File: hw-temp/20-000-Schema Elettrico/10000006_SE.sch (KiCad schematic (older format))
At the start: 36 parts, among them P1 CONN_01X04, P2 CONN_01X04, P3 CONN_01X04, P4 CONN_01X04, P5 CONN_01X04, P6 CONN_01X04, P7 CONN_01X04, P8 CONN_01X04, U1 TPS709, U2 PCA9306DC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

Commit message: aggiornamento completo libreria e schematico per generazione BOM
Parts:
- removed C1: 1u, symbol C
- removed C2: 3.3u, symbol C
- removed C3, C5, C7, C8, C9: 100n, symbol C
- removed C4, C6: 100p, symbol C
- removed P1, P2, P3, P4, P5, P6, P7, P8: CONN_01X04, symbol CONN_01X04
- added C1: C_1u_0603_10_X7R_25V, Capacitors_SMD:C_0603, symbol C_1u_0603_10_X7R_25V
- added C2: C_3u3_0603_10_X5R_10V, Capacitors_SMD:C_0603, symbol C_3u3_0603_10_X5R_10V
- added C3, C5, C7, C8, C9: C_100n_0603_10_X7R_25V, Capacitors_SMD:C_0603, symbol C_100n_0603_10_X7R_25V
- added C4, C6: C_100p_0603_5_NP0_50V, Capacitors_SMD:C_0603, symbol C_100p_0603_5_NP0_50V
- added P1, P2, P3, P4, P5, P6, P7, P8: PLUG_01X04_254, Socket_Strips:Socket_Strip_Straight_1x04, symbol PLUG_01X04_254
- U1: footprint (none) -> TO_SOT_Packages_SMD:SOT-23-5; MF (none) -> TI; MF_PN (none) -> TPS709; NOPOP (none) -> 0; VAL (none) -> TPS709
- U2: footprint (none) -> Housings_SSOP:TSSOP-8_3x3mm_Pitch0.65mm; MF (none) -> TI; MF_PN (none) -> PCA9306DCUR; NOPOP (none) -> 0; VAL (none) -> PCA9306DC
- U3: footprint (none) -> Housings_SSOP:TSSOP-16_4.4x5mm_Pitch0.65mm; MF (none) -> NXP; MF_PN (none) -> SC18IS602BIPW,128; NOPOP (none) -> 0; VAL (none) -> SC18IS602BIPW
- U4: footprint (none) -> Housings_SSOP:SSOP-20_5.3x7.2mm_Pitch0.65mm; MF (none) -> Maxim; MF_PN (none) -> MAX31865AAP+; NOPOP (none) -> 0; VAL (none) -> MAX31865

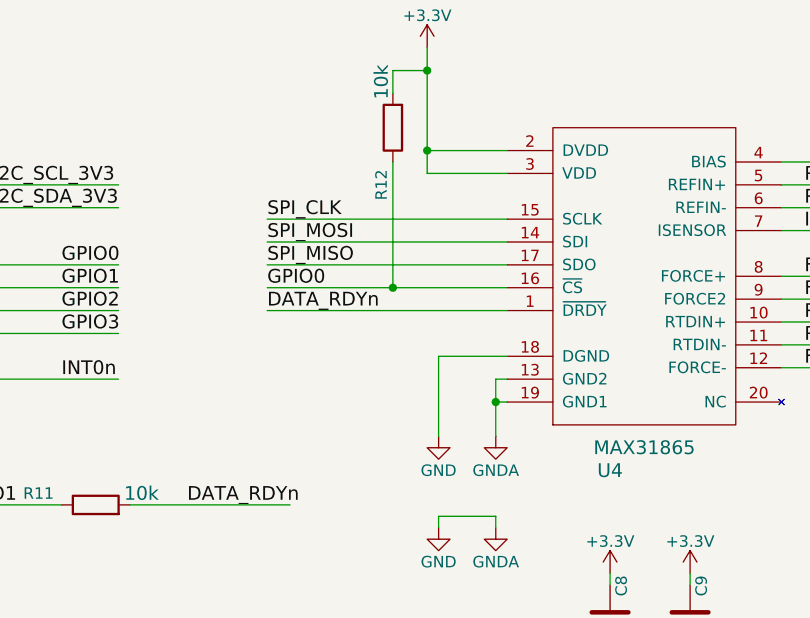
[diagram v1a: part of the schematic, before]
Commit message: Piazzamento scheda iniziato
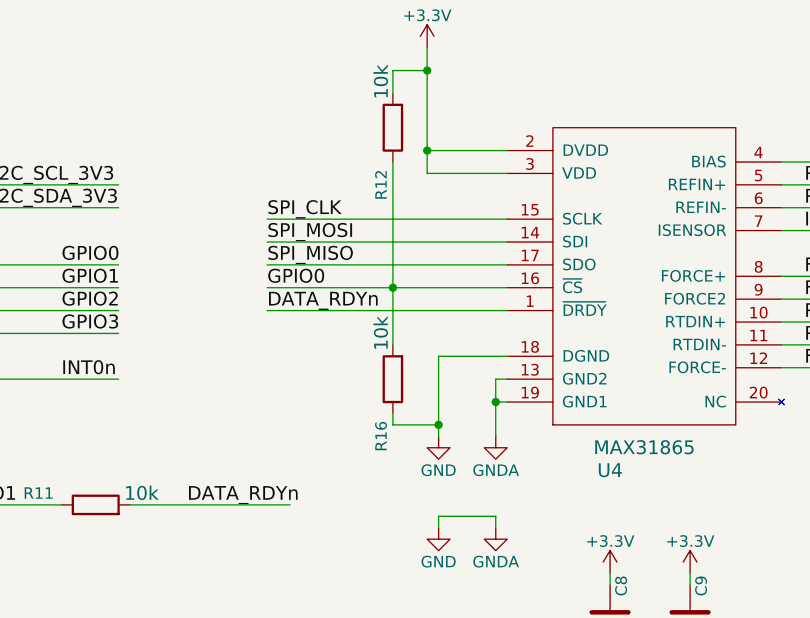
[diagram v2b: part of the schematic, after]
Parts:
- added R16: R_10K_0603_5, Resistors_SMD:R_0603, symbol R_10K_0603_5
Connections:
- wire segments 153 -> 155
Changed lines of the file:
@@
 01
 $Comp
-L GND #PWR01
+L GND #PWR7
 U 1 1 568A9F3F
 P 2050 2350
-F 0 "#PWR01" H 2050 2100 50  0001 C CNN
+F 0 "#PWR7" H 2050 2100 50  0001 C CNN
 F 1 "GND" H 2050 2200 50  0000 C CNN
 F 2 "" H 2050 2350 50  0000 C CNN
@@
 $EndComp
 $Comp
-L +3.3V #PWR02
+L +3.3V #PWR6
 U 1 1 568A9F53
 P 2050 2000
-F 0 "#PWR02" H 2050 1850 50  0001 C CNN
+F 0 "#PWR6" H 2050 1850 50  0001 C CNN
 F 1 "+3.3V" H 2050 2140 50  0000 C CNN
 F 2 "" H 2050 2000 50  0000 C CNN
@@
 $EndComp
 $Comp
-L +5V #PWR03
+L +5V #PWR5
 U 1 1 568A9F67
 P 2050 1650
-F 0 "#PWR03" H 2050 1500 50  0001 C CNN
+F 0 "#PWR5" H 2050 1500 50  0001 C CNN
 F 1 "+5V" H 2050 1790 50  0000 C CNN
 F 2 "" H 2050 1650 50  0000 C CNN
@@
 $EndComp
 $Comp
-L PWR_FLAG #FLG04
+L PWR_FLAG #FLG2
 U 1 1 568A9F7B
 P 1700 2000
-F 0 "#FLG04" H 1700 2095 50  0001 C CNN
+F 0 "#FLG2" H 1700 2095 50  0001 C CNN
 F 1 "PWR_FLAG" H 1700 2180 50  0000 C CNN
 F 2 "" H 1700 2000 50  0000 C CNN
@@
 $EndComp
 $Comp
-L PWR_FLAG #FLG05
+L PWR_FLAG #FLG1
 U 1 1 568A9F8F
 P 1700 1650
-F 0 "#FLG05" H 1700 1745 50  0001 C CNN
+F 0 "#FLG1" H 1700 1745 50  0001 C CNN
 F 1 "PWR_FLAG" H 1700 1830 50  0000 C CNN
 F 2 "" H 1700 1650 50  0000 C CNN
@@
 $EndComp
 $Comp
-L PWR_FLAG #FLG06
+L PWR_FLAG #FLG3
 U 1 1 568A9FA3
 P 1700 2350
-F 0 "#FLG06" H 1700 2445 50  0001 C CNN
+F 0 "#FLG3" H 1700 2445 50  0001 C CNN
 F 1 "PWR_FLAG" H 1700 2530 50  0000 C CNN
 F 2 "" H 1700 2350 50  0000 C CNN
@@
 $EndComp
 $Comp
-L PWR_FLAG #FLG07
+L PWR_FLAG #FLG4
 U 1 1 568AA6D7
 P 1700 2750
-F 0 "#FLG07" H 1700 2845 50  0001 C CNN
+F 0 "#FLG4" H 1700 2845 50  0001 C CNN
 F 1 "PWR_FLAG" H 1700 2930 50  0000 C CNN
 F 2 "" H 1700 2750 50  0000 C CNN
@@
 $EndComp
 $Comp
-L GNDA #PWR08
+L GNDA #PWR8
 U 1 1 568AA6F4
 P 2050 2750
-F 0 "#PWR08" H 2050 2500 50  0001 C CNN
+F 0 "#PWR8" H 2050 2500 50  0001 C CNN
 F 1 "GNDA" H 2050 2600 50  0000 C CNN
 F 2 "" H 2050 2750 50  0000 C CNN
@@
 $EndComp
 $Comp
-L +5V #PWR09
+L +5V #PWR3
 U 1 1 568AAB25
 P 1350 6100
-F 0 "#PWR09" H 1350 5950 50  0001 C CNN
+F 0 "#PWR3" H 1350 5950 50  0001 C CNN
 F 1 "+5V" H 1350 6240 50  0000 C CNN
 F 2 "" H 1350 6100 50  0000 C CNN
@@
 $EndComp
 $Comp
-L GND #PWR010
+L GND #PWR4
 U 1 1 568AAC28
 P 1350 6500
-F 0 "#PWR010" H 1350 6250 50  0001 C CNN
+F 0 "#PWR4" H 1350 6250 50  0001 C CNN
 F 1 "GND" H 1350 6350 50  0000 C CNN
 F 2 "" H 1350 6500 50  0000 C CNN
@@
 FORCE_N
 $Comp
-L +5V #PWR011
+L +5V #PWR11
 U 1 1 568AAF5E
 P 3250 6100
-F 0 "#PWR011" H 3250 5950 50  0001 C CNN
+F 0 "#PWR11" H 3250 5950 50  0001 C CNN
 F 1 "+5V" H 3250 6240 50  0000 C CNN
 F 2 "" H 3250 6100 50  0000 C CNN
@@
 $EndComp
 $Comp
-L GND #PWR012
+L GND #PWR12
 U 1 1 568AAF64
 P 3250 6500
-F 0 "#PWR012" H 3250 6250 50  0001 C CNN
+F 0 "#PWR12" H 3250 6250 50  0001 C CNN
 F 1 "GND" H 3250 6350 50  0000 C CNN
 F 2 "" H 3250 6500 50  0000 C CNN
@@
 I2C_SDA
 $Comp
-L +5V #PWR013
+L +5V #PWR18
 U 1 1 568AB074
 P 4700 6100
-F 0 "#PWR013" H 4700 5950 50  0001 C CNN
+F 0 "#PWR18" H 4700 5950 50  0001 C CNN
 F 1 "+5V" H 4700 6240 50  0000 C CNN
 F 2 "" H 4700 6100 50  0000 C CNN
@@
 $EndComp
 $Comp
-L GND #PWR014
+L GND #PWR19
 U 1 1 568AB07A
 P 4700 6500
-F 0 "#PWR014" H 4700 6250 50  0001 C CNN
+F 0 "#PWR19" H 4700 6250 50  0001 C CNN
 F 1 "GND" H 4700 6350 50  0000 C CNN
 F 2 "" H 4700 6500 50  0000 C CNN
@@
 NoConn ~ 5400 7250
 $Comp
-L GND #PWR015
+L GND #PWR2
 U 1 1 568C08DA
 P 1300 4950
-F 0 "#PWR015" H 1300 4700 50  0001 C CNN
+F 0 "#PWR2" H 1300 4700 50  0001 C CNN
 F 1 "GND" H 1300 4800 50  0000 C CNN
 F 2 "" H 1300 4950 50  0000 C CNN
@@
 $EndComp
 $Comp
-L GND #PWR016
+L GND #PWR10
 U 1 1 568C090F
 P 2900 4950
-F 0 "#PWR016" H 2900 4700 50  0001 C CNN
+F 0 "#PWR10" H 2900 4700 50  0001 C CNN
 F 1 "GND" H 2900 4800 50  0000 C CNN
 F 2 "" H 2900 4950 50  0000 C CNN
@@
 $EndComp
 $Comp
-L +5V #PWR017
+L +5V #PWR1
 U 1 1 568C0944
 P 1300 4150
-F 0 "#PWR017" H 1300 4000 50  0001 C CNN
+F 0 "#PWR1" H 1300 4000 50  0001 C CNN
 F 1 "+5V" H 1300 4290 50  0000 C CNN
 F 2 "" H 1300 4150 50  0000 C CNN
@@
 $EndComp
 $Comp
-L +3.3V #PWR018
+L +3.3V #PWR9
 U 1 1 568C0E2D
 P 2900 4150
-F 0 "#PWR018" H 2900 4000 50  0001 C CNN
+F 0 "#PWR9" H 2900 4000 50  0001 C CNN
 F 1 "+3.3V" H 2900 4290 50  0000 C CNN
 F 2 "" H 2900 4150 50  0000 C CNN
@@
 NoConn ~ 1650 4550
 $Comp
-L GND #PWR019
+L GND #PWR22
 U 1 1 568C15F2
 P 6300 4850
-F 0 "#PWR019" H 6300 4600 50  0001 C CNN
+F 0 "#PWR22" H 6300 4600 50  0001 C CNN
 F 1 "GND" H 6300 4700 50  0000 C CNN
 F 2 "" H 6300 4850 50  0000 C CNN
@@
 $EndComp
 $Comp
-L +5V #PWR020
+L +5V #PWR21
 U 1 1 568C15F8
 P 6300 4050
-F 0 "#PWR020" H 6300 3900 50  0001 C CNN
+F 0 "#PWR21" H 6300 3900 50  0001 C CNN
 F 1 "+5V" H 6300 4190 50  0000 C CNN
 F 2 "" H 6300 4050 50  0000 C CNN
@@
 $EndComp
 $Comp
-L GND #PWR021
+L GND #PWR17
 U 1 1 568C183D
 P 4200 4800
-F 0 "#PWR021" H 4200 4550 50  0001 C CNN
+F 0 "#PWR17" H 4200 4550 50  0001 C CNN
 F 1 "GND" H 4200 4650 50  0000 C CNN
 F 2 "" H 4200 4800 50  0000 C CNN
@@
 $EndComp
 $Comp
-L +5V #PWR022
+L +5V #PWR13
 U 1 1 568C1878
 P 3900 4150
-F 0 "#PWR022" H 3900 4000 50  0001 C CNN
+F 0 "#PWR13" H 3900 4000 50  0001 C CNN
 F 1 "+5V" H 3900 4290 50  0000 C CNN
 F 2 "" H 3900 4150 50  0000 C CNN
@@
 $EndComp
 $Comp
-L +3.3V #PWR023
+L +3.3V #PWR16
 U 1 1 568C18B3
 P 4150 4150
-F 0 "#PWR023" H 4150 4000 50  0001 C CNN
+F 0 "#PWR16" H 4150 4000 50  0001 C CNN
 F 1 "+3.3V" H 4150 4290 50  0000 C CNN
 F 2 "" H 4150 4150 50  0000 C CNN
@@
 I2C_SDA
 $Comp
-L GND #PWR024
+L GND #PWR24
 U 1 1 568C2337
 P 7000 4850
-F 0 "#PWR024" H 7000 4600 50  0001 C CNN
+F 0 "#PWR24" H 7000 4600 50  0001 C CNN
 F 1 "GND" H 7000 4700 50  0000 C CNN
 F 2 "" H 7000 4850 50  0000 C CNN
@@
 $EndComp
 $Comp
-L +3.3V #PWR025
+L +3.3V #PWR23
 U 1 1 568C23B3
 P 7000 4050
-F 0 "#PWR025" H 7000 3900 50  0001 C CNN
+F 0 "#PWR23" H 7000 3900 50  0001 C CNN
 F 1 "+3.3V" H 7000 4190 50  0000 C CNN
 F 2 "" H 7000 4050 50  0000 C CNN
@@
 $EndComp
 $Comp
-L +3.3V #PWR026
+L +3.3V #PWR14
 U 1 1 568C2718
 P 3950 950
-F 0 "#PWR026" H 3950 800 50  0001 C CNN
+F 0 "#PWR14" H 3950 800 50  0001 C CNN
 F 1 "+3.3V" H 3950 1090 50  0000 C CNN
 F 2 "" H 3950 950 50  0000 C CNN
@@
 $EndComp
 $Comp
-L GND #PWR027
+L GND #PWR15
 U 1 1 568C2BD0
 P 4150 2700
-F 0 "#PWR027" H 4150 2450 50  0001 C CNN
+F 0 "#PWR15" H 4150 2450 50  0001 C CNN
 F 1 "GND" H 4150 2550 50  0000 C CNN
 F 2 "" H 4150 2700 50  0000 C CNN
@@
 SPI_MOSI
 $Comp
-L +3.3V #PWR028
+L +3.3V #PWR20
 U 1 1 568C4E4E
 P 6000 900
-F 0 "#PWR028" H 6000 750 50  0001 C CNN
+F 0 "#PWR20" H 6000 750 50  0001 C CNN
 F 1 "+3.3V" H 6000 1040 50  0000 C CNN
 F 2 "" H 6000 900 50  0000 C CNN
@@
 GPIO3
 $Comp
-L GND #PWR029
+L GND #PWR26
 U 1 1 568C62D5
 P 8200 2750
-F 0 "#PWR029" H 8200 2500 50  0001 C CNN
+F 0 "#PWR26" H 8200 2500 50  0001 C CNN
 F 1 "GND" H 8200 2600 50  0000 C CNN
 F 2 "" H 8200 2750 50  0000 C CNN
@@
 $EndComp
 $Comp
-L GNDA #PWR030
+L GNDA #PWR28
 U 1 1 568C6334
 P 8450 2750
-F 0 "#PWR030" H 8450 2500 50  0001 C CNN
+F 0 "#PWR28" H 8450 2500 50  0001 C CNN
 F 1 "GNDA" H 8450 2600 50  0000 C CNN
 F 2 "" H 8450 2750 50  0000 C CNN
@@
 $EndComp
 $Comp
-L GND #PWR031
+L GND #PWR27
 U 1 1 568C6AA4
 P 8200 3150
-F 0 "#PWR031" H 8200 2900 50  0001 C CNN
+F 0 "#PWR27" H 8200 2900 50  0001 C CNN
 F 1 "GND" H 8200 3000 50  0000 C CNN
 F 2 "" H 8200 3150 50  0000 C CNN
@@
 $EndComp
 $Comp
-L GNDA #PWR032
+L GNDA #PWR29
 U 1 1 568C6AAA
 P 8450 3150
-F 0 "#PWR032" H 8450 2900 50  0001 C CNN
+F 0 "#PWR29" H 8450 2900 50  0001 C CNN
 F 1 "GNDA" H 8450 3000 50  0000 C CNN
 F 2 "" H 8450 3150 50  0000 C CNN
@@
 $EndComp
 $Comp
-L +3.3V #PWR033
+L +3.3V #PWR30
 U 1 1 568C6C12
 P 8950 3350
-F 0 "#PWR033" H 8950 3200 50  0001 C CNN
+F 0 "#PWR30" H 8950 3200 50  0001 C CNN
 F 1 "+3.3V" H 8950 3490 50  0000 C CNN
 F 2 "" H 8950 3350 50  0000 C CNN
@@
 $EndComp
 $Comp
-L GND #PWR034
+L GND #PWR31
 U 1 1 568C6C74
 P 8950 3800
-F 0 "#PWR034" H 8950 3550 50  0001 C CNN
+F 0 "#PWR31" H 8950 3550 50  0001 C CNN
 F 1 "GND" H 8950 3650 50  0000 C CNN
 F 2 "" H 8950 3800 50  0000 C CNN
@@
 $EndComp
 $Comp
-L +3.3V #PWR035
+L +3.3V #PWR32
 U 1 1 568C6CF5
 P 9300 3350
-F 0 "#PWR035" H 9300 3200 50  0001 C CNN
+F 0 "#PWR32" H 9300 3200 50  0001 C CNN
 F 1 "+3.3V" H 9300 3490 50  0000 C CNN
 F 2 "" H 9300 3350 50  0000 C CNN
@@
 $EndComp
 $Comp
-L GNDA #PWR036
+L GNDA #PWR33
 U 1 1 568C6D97
 P 9300 3800
-F 0 "#PWR036" H 9300 3550 50  0001 C CNN
+F 0 "#PWR33" H 9300 3550 50  0001 C CNN
 F 1 "GNDA" H 9300 3650 50  0000 C CNN
 F 2 "" H 9300 3800 50  0000 C CNN
@@
 $EndComp
 $Comp
-L +3.3V #PWR037
+L +3.3V #PWR25
 U 1 1 568C758B
 P 8150 1050
-F 0 "#PWR037" H 8150 900 50  0001 C CNN
+F 0 "#PWR25" H 8150 900 50  0001 C CNN
 F 1 "+3.3V" H 8150 1190 50  0000 C CNN
 F 2 "" H 8150 1050 50  0000 C CNN
@@
 	7450 2100 8500 2100
 Wire Wire Line
-	8000 2100 8000 1550
+	8000 1550 8000 2350
 Wire Wire Line
 	8000 1250 8000 1150
@@
 FORCE2
 $Comp
-L GNDA #PWR038
+L GNDA #PWR34
 U 1 1 568CDDF1
 P 10300 5050
-F 0 "#PWR038" H 10300 4800 50  0001 C CNN
+F 0 "#PWR34" H 10300 4800 50  0001 C CNN
 F 1 "GNDA" H 10300 4900 50  0000 C CNN
 F 2 "" H 10300 5050 50  0000 C CNN
@@
 	1    0    0    -1
 $EndComp
+$Comp
+L R_10K_0603_5 R16
+U 1 1 56A02B34
+P 8000 2500
+F 0 "R16" V 8050 2750 50  0000 C CNN
+F 1 "R_10K_0603_5" V 8000 2500 50  0001 C CNN
+F 2 "Resistors_SMD:R_0603" V 7930 2500 50  0001 C CNN
+F 3 "" V 8080 2500 50  0000 C CNN
+F 4 "0" V 8180 2600 60  0001 C CNN "NOPOP"
+F 5 "KOA Spear" V 8280 2700 60  0001 C CNN "MF"
+F 6 "RK73B1JTTD103J" V 8380 2800 60  0001 C CNN "MF_PN"
+F 7 "10k" V 8050 2300 60  0000 C CNN "VAL"
+	1    8000 2500
+	-1   0    0    1
+$EndComp
+Wire Wire Line
+	8000 2650 8000 2700
+Wire Wire Line
+	8000 2700 8200 2700
+Connection ~ 8200 2700
 $EndSCHEMATC

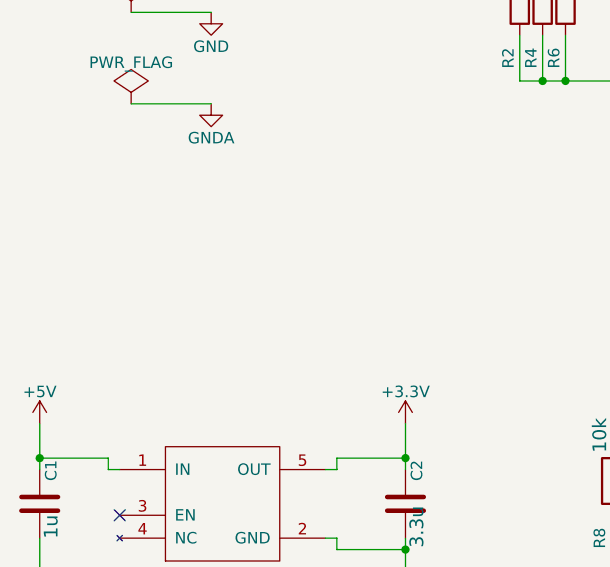
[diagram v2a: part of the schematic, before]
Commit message: completato schema elettrico e sbroglio
Signed-off-by: CrazyDiamond <crazyd14@gmail.com>
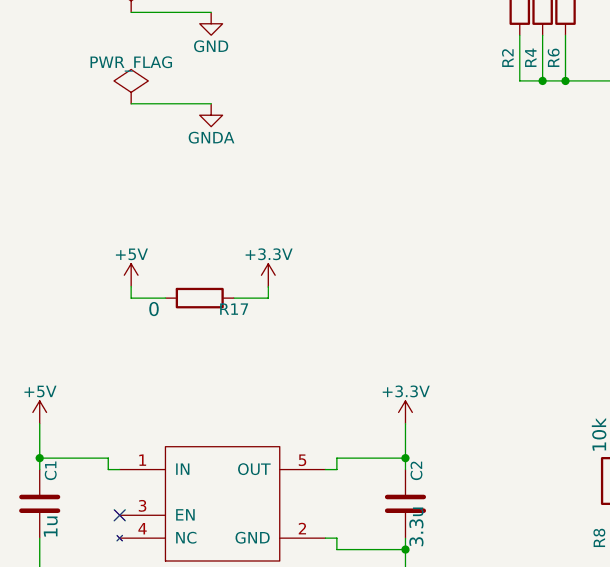
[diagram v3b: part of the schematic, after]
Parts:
- added R17: R_0_0603_5, Resistors_SMD:R_0603, symbol R_0_0603_5
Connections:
- wire segments 155 -> 159

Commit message: PCB terminato
Signed-off-by: CrazyDiamond <crazyd14@gmail.com>
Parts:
- removed P1, P2: PLUG_01X04_254, Socket_Strips:Socket_Strip_Straight_1x04, symbol PLUG_01X04_254
- added P1, P2: TERMINAL_01X04_250_RA_SPRING, os_terminal_block:1770908, symbol TERMINAL_01X04_250_RA_SPRING
